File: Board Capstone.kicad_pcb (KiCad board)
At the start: 2 copper layers, 100 x 79 mm, 59 parts, among them J101 JST-ZH 4P, J102 HDR 02x20 2.54, J103 JST-ZH 2P, J104 JST-ZH 2P, J105 JST-ZH 3P, J106 JST-ZH 3P, J201 JST-XH 6P, Q101 FDV304P, Q102 BC847CLT3G, Q103 MMBT2907AL, Q104 MMBT2907AL, Q201 FDV301N, Q202 FDV301N, Q203 SSF3365, SW201 SW, U101 MCP3021, U102 SN74LV1T125DBV, U103 SN74LV1T125DBV, U201 LM2678SX-5.0, U202 BQ7720700DSSR, U203 LM2675M-12

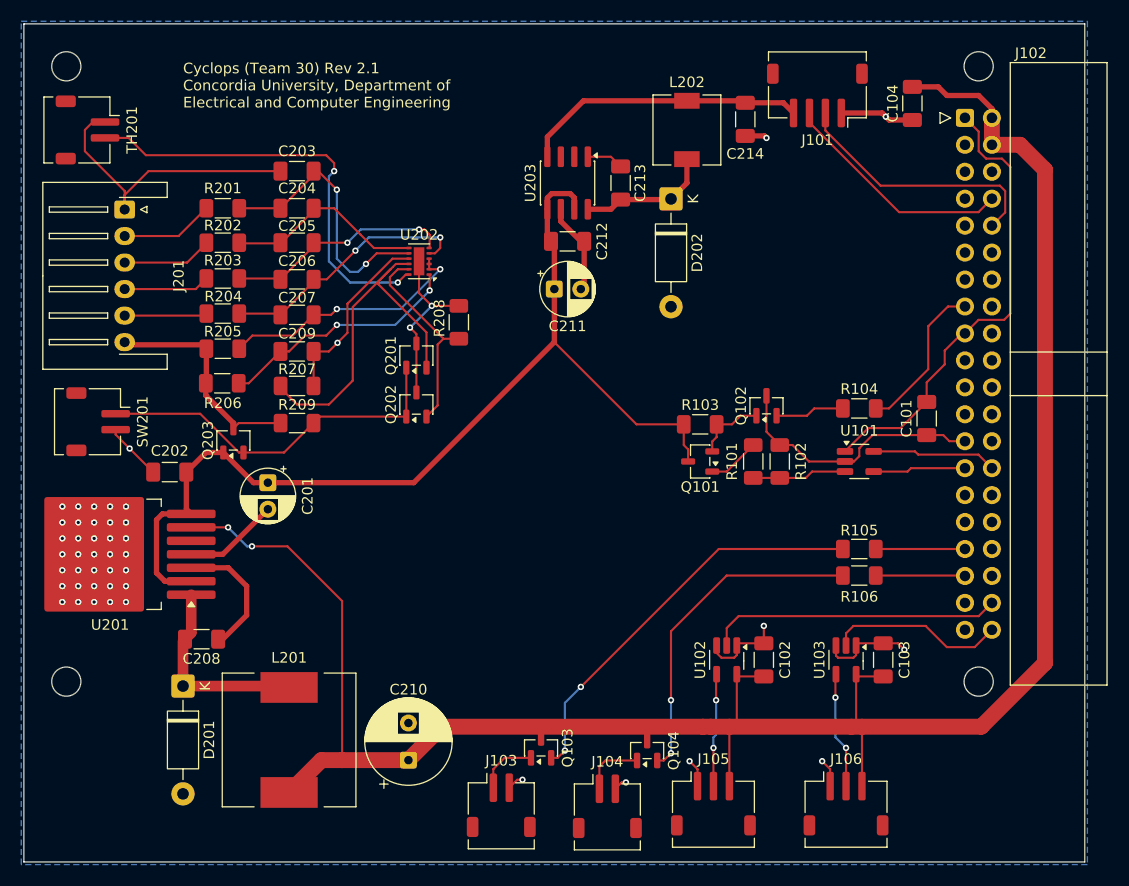
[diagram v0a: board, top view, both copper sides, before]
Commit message: Rev 2.2 Added test point and status LED
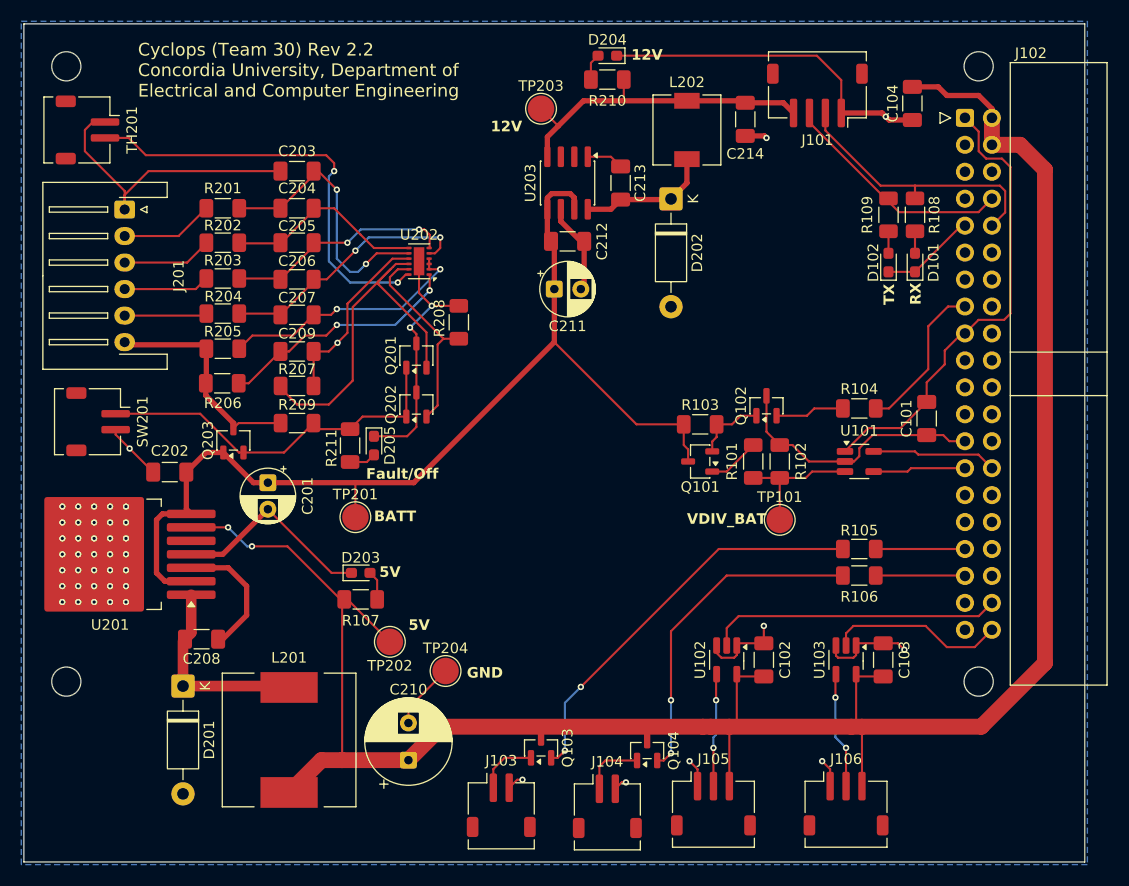
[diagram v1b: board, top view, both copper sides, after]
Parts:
- added D101: AMBER, LED_SMD:LED_0603_1608Metric_Pad1.05x0.95mm_HandSolder, F.Cu at (134.0, 72.5)
- added D102: AMBER, LED_SMD:LED_0603_1608Metric_Pad1.05x0.95mm_HandSolder, F.Cu at (131.5, 72.5)
- added D203: RED, LED_SMD:LED_0603_1608Metric_Pad1.05x0.95mm_HandSolder, F.Cu at (81.8, 101.8)
- added D204: RED, LED_SMD:LED_0603_1608Metric_Pad1.05x0.95mm_HandSolder, F.Cu at (105.0, 53.0)
- added D205: RED, LED_SMD:LED_0603_1608Metric_Pad1.05x0.95mm_HandSolder, F.Cu at (83.0, 89.8)
- added R107: 5k, Resistor_SMD:R_1206_3216Metric_Pad1.30x1.75mm_HandSolder, F.Cu at (81.8, 104.2)
- added R108: 1.5k, Resistor_SMD:R_1206_3216Metric_Pad1.30x1.75mm_HandSolder, F.Cu at (134.0, 68.0)
- added R109: 1.5k, Resistor_SMD:R_1206_3216Metric_Pad1.30x1.75mm_HandSolder, F.Cu at (131.5, 68.0)
- added R210: 12k, Resistor_SMD:R_1206_3216Metric_Pad1.30x1.75mm_HandSolder, F.Cu at (105.0, 55.2)
- added R211: 20k, Resistor_SMD:R_1206_3216Metric_Pad1.30x1.75mm_HandSolder, F.Cu at (80.8, 89.8)
- added TP101: ~, TestPoint:TestPoint_Pad_D2.5mm, F.Cu at (121.2, 96.8)
- added TP201: ~, TestPoint:TestPoint_Pad_D2.5mm, F.Cu at (81.2, 96.5)
- added TP202: ~, TestPoint:TestPoint_Pad_D2.5mm, F.Cu at (84.5, 108.2)
- added TP203: ~, TestPoint:TestPoint_Pad_D2.5mm, F.Cu at (98.8, 58.0)
- added TP204: GND, TestPoint:TestPoint_Pad_D2.5mm, F.Cu at (89.8, 111.0)
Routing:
- net GND: track 144.5 -> 203.1 mm
- net +5V: track 199.4 -> 205.4 mm
- net +12V: track 27.0 -> 31.3 mm
- net Net-(U101-AIN): track 8.90 -> 12.8 mm
- net +BATT: track 95.3 -> 98.6 mm
- net Net-(D203-A): track 0.00 -> 2.78 mm
- net Net-(D205-A): track 0.00 -> 2.53 mm
- net Net-(D204-A): track 0.00 -> 2.53 mm
- net Net-(D102-A): track 0.00 -> 2.08 mm
- net Net-(D101-A): track 0.00 -> 2.08 mm
- net /UART_RX: track 24.7 -> 25.9 mm
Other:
- board text added: "12V"
- board text added: "5V"
- board text added: "BATT"
- board text added: "Cyclops (Team 30) Rev 2.2 Concordia University, Department of Electrical and Computer Engineering"
- board text added: "Fault/Off"
- board text added: "GND"
- board text added: "RX"
- board text added: "TX"
- board text added: "VDIV_BAT"
- board text removed: "Cyclops (Team 30) Rev 2.1 Concordia University, Department of Electrical and Computer Engineering"

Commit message: Rev 2.4
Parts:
- removed C101, C102, C103, C203, C204, C205, C206, C207, C209: 0.1uF, Capacitor_SMD:C_1206_3216Metric_Pad1.33x1.80mm_HandSolder
- removed C104: 10uF, Capacitor_SMD:C_1206_3216Metric_Pad1.33x1.80mm_HandSolder
- removed C201, C211: 15uF, Capacitor_THT:CP_Radial_D5.0mm_P2.50mm
- removed C202, C212: 1uF, Capacitor_SMD:C_1206_3216Metric_Pad1.33x1.80mm_HandSolder
- removed C208, C213: 0.01uF, Capacitor_SMD:C_1206_3216Metric_Pad1.33x1.80mm_HandSolder
- removed C210: 180uF, Capacitor_THT:CP_Radial_D8.0mm_P3.50mm
- removed C214: 47uF, Capacitor_SMD:C_1206_3216Metric_Pad1.33x1.80mm_HandSolder
- removed D101, D102: AMBER, LED_SMD:LED_0603_1608Metric_Pad1.05x0.95mm_HandSolder
- removed D201, D202: ~, Diode_THT:D_DO-41_SOD81_P10.16mm_Horizontal
- removed D203, D204, D205: RED, LED_SMD:LED_0603_1608Metric_Pad1.05x0.95mm_HandSolder
- removed J101: JST-ZH 4P, Connector_JST:JST_ZH_S4B-ZR-SM4A-TF_1x04-1MP_P1.50mm_Horizontal
- removed J103, J104: JST-ZH 2P, Connector_JST:JST_ZH_S2B-ZR-SM4A-TF_1x02-1MP_P1.50mm_Horizontal
- removed J105, J106: JST-ZH 3P, Connector_JST:JST_ZH_S3B-ZR-SM4A-TF_1x03-1MP_P1.50mm_Horizontal
- removed J201: JST-XH 6P, Connector_JST:JST_XH_S6B-XH-A-1_1x06_P2.50mm_Horizontal
- removed L201: 22uH, Inductor_SMD:L_12x12mm_H4.5mm
- removed L202: 22uH, Inductor_SMD:L_6.3x6.3_H3
- removed Q101: FDV304P, Package_TO_SOT_SMD:SOT-23-3
- removed Q102: BC847CLT3G, Package_TO_SOT_SMD:SOT-23
- removed Q103, Q104: MMBT2907AL, Package_TO_SOT_SMD:SOT-23
- removed Q201, Q202: FDV301N, Package_TO_SOT_SMD:SOT-23-3
- removed Q203: SSF3365, Package_TO_SOT_SMD:SOT-23-3
- removed R101, R103, R207, R208, R209: 10k, Resistor_SMD:R_1206_3216Metric_Pad1.30x1.75mm_HandSolder
- removed R102, R104, R105, R106, R201, R202, R203, R204, R205: 1k, Resistor_SMD:R_1206_3216Metric_Pad1.30x1.75mm_HandSolder
- removed R107: 5k, Resistor_SMD:R_1206_3216Metric_Pad1.30x1.75mm_HandSolder
- removed R108, R109: 1.5k, Resistor_SMD:R_1206_3216Metric_Pad1.30x1.75mm_HandSolder
- removed R206: 300, Resistor_SMD:R_1206_3216Metric_Pad1.30x1.75mm_HandSolder
- removed R210: 12k, Resistor_SMD:R_1206_3216Metric_Pad1.30x1.75mm_HandSolder
- removed R211: 20k, Resistor_SMD:R_1206_3216Metric_Pad1.30x1.75mm_HandSolder
- removed SW201: SW, Connector_JST:JST_ZH_S2B-ZR-SM4A-TF_1x02-1MP_P1.50mm_Horizontal
- removed TH201: NTC 10k, Connector_JST:JST_ZH_S2B-ZR-SM4A-TF_1x02-1MP_P1.50mm_Horizontal
- removed TP101, TP201, TP202, TP203: ~, TestPoint:TestPoint_Pad_D2.5mm
- removed TP204: GND, TestPoint:TestPoint_Pad_D2.5mm
- removed U101: MCP3021, Package_TO_SOT_SMD:SOT-23-5_HandSoldering
- removed U102, U103: SN74LV1T125DBV, Package_TO_SOT_SMD:SOT-23-5_HandSoldering
- removed U201: LM2678SX-5.0, Package_TO_SOT_SMD:TO-263-7_TabPin4
- removed U202: BQ7720700DSSR, Package_SON:WSON-12-1EP_3x2mm_P0.5mm_EP1x2.65
- removed U203: LM2675M-12, Package_SO:SOIC-8_3.9x4.9mm_P1.27mm
- added C1: 10uF, Capacitor_SMD:C_0805_2012Metric_Pad1.18x1.45mm_HandSolder, F.Cu at (77.5, 118.2)
- added C10: 1uF, Capacitor_SMD:C_0805_2012Metric_Pad1.18x1.45mm_HandSolder, F.Cu at (102.5, 116.5)
- added C11: 47uF, Capacitor_SMD:C_0805_2012Metric_Pad1.18x1.45mm_HandSolder, F.Cu at (105.8, 84.5)
- added C12: 220nF, Capacitor_SMD:C_0805_2012Metric_Pad1.18x1.45mm_HandSolder, F.Cu at (72.5, 75.0)
- added C13: 220nF, Capacitor_SMD:C_0805_2012Metric_Pad1.18x1.45mm_HandSolder, F.Cu at (72.5, 72.5)
- added C14: 220nF, Capacitor_SMD:C_0805_2012Metric_Pad1.18x1.45mm_HandSolder, F.Cu at (72.5, 70.0)
- added C15: 220nF, Capacitor_SMD:C_0805_2012Metric_Pad1.18x1.45mm_HandSolder, F.Cu at (72.5, 67.5)
- added C16: 220nF, Capacitor_SMD:C_0805_2012Metric_Pad1.18x1.45mm_HandSolder, F.Cu at (72.5, 65.0)
- added C17: 220nF, Capacitor_SMD:C_0805_2012Metric_Pad1.18x1.45mm_HandSolder, F.Cu at (72.5, 62.5)
- added C18: 1uF, Capacitor_SMD:C_0805_2012Metric_Pad1.18x1.45mm_HandSolder, F.Cu at (109.2, 84.5)
- added C19: 220nF, Capacitor_SMD:C_0805_2012Metric_Pad1.18x1.45mm_HandSolder, F.Cu at (72.5, 77.5)
- added C2: 0.1uF, Capacitor_SMD:C_0805_2012Metric_Pad1.18x1.45mm_HandSolder, F.Cu at (111.8, 91.2)
- added C20: 0.01uF, Capacitor_SMD:C_0805_2012Metric_Pad1.18x1.45mm_HandSolder, F.Cu at (116.2, 72.2)
- added C21: 1uF, Capacitor_SMD:C_0805_2012Metric_Pad1.18x1.45mm_HandSolder, F.Cu at (87.2, 72.8)
- added C22: 100pF, Capacitor_SMD:C_0805_2012Metric_Pad1.18x1.45mm_HandSolder, F.Cu at (84.2, 85.2)
- added C23: 180uF, Capacitor_THT:CP_Radial_D8.0mm_P3.50mm, F.Cu at (118.0, 57.0)
- added C24: 1uF, Capacitor_SMD:C_0805_2012Metric_Pad1.18x1.45mm_HandSolder, F.Cu at (82.8, 72.8)
- added C25: 47uF, Capacitor_SMD:C_0805_2012Metric_Pad1.18x1.45mm_HandSolder, F.Cu at (75.5, 107.5)
- added C26: 1uF, Capacitor_SMD:C_0805_2012Metric_Pad1.18x1.45mm_HandSolder, F.Cu at (71.5, 107.5)
- added C27: 0.01uF, Capacitor_SMD:C_0805_2012Metric_Pad1.18x1.45mm_HandSolder, F.Cu at (65.5, 113.5)
- added C28: 47uF, Capacitor_SMD:C_0805_2012Metric_Pad1.18x1.45mm_HandSolder, F.Cu at (75.5, 113.5)
- added C29: 1uF, Capacitor_SMD:C_0805_2012Metric_Pad1.18x1.45mm_HandSolder, F.Cu at (117.2, 98.2)
- added C3: 1uF, Capacitor_SMD:C_0805_2012Metric_Pad1.18x1.45mm_HandSolder, F.Cu at (121.7, 115.0)
- added C4: 1uF, Capacitor_SMD:C_0805_2012Metric_Pad1.18x1.45mm_HandSolder, F.Cu at (136.5, 115.0)
- added C5: 1uF, Capacitor_SMD:C_0805_2012Metric_Pad1.18x1.45mm_HandSolder, F.Cu at (135.5, 63.0)
- added C6: 10uF, Capacitor_SMD:C_0805_2012Metric_Pad1.18x1.45mm_HandSolder, F.Cu at (135.5, 59.0)
- added C7: 0.1uF, Capacitor_SMD:C_0805_2012Metric_Pad1.18x1.45mm_HandSolder, F.Cu at (91.5, 111.5)
- added C8: 0.1uF, Capacitor_SMD:C_0805_2012Metric_Pad1.18x1.45mm_HandSolder, F.Cu at (106.5, 111.5)
- added C9: 1uF, Capacitor_SMD:C_0805_2012Metric_Pad1.18x1.45mm_HandSolder, F.Cu at (87.5, 116.5)
- added D10: D_Zener, Diode_SMD:D_0805_2012Metric_Pad1.15x1.40mm_HandSolder, F.Cu at (117.2, 101.2)
- added D3: 1N4148W, Diode_SMD:D_SOD-123, F.Cu at (86.5, 64.5)
- added D4: SK35, Diode_SMD:D_SMB-SMC_Universal_Handsoldering, F.Cu at (117.0, 67.0)
- added D5: 1N4148W, Diode_SMD:D_SOD-123, F.Cu at (83.5, 64.5)
- added D7: SK15, Diode_SMD:D_SMA-SMB_Universal_Handsoldering, F.Cu at (61.0, 106.5)
- added D8: QBLP601-R35, LED_SMD:LED_0603_1608Metric_Pad1.05x0.95mm_HandSolder, F.Cu at (97.0, 83.0)
- added J1: JST-ZH 4P, Connector_JST:JST_ZH_S4B-ZR-SM4A-TF_1x04-1MP_P1.50mm_Horizontal, F.Cu at (72.5, 123.0)
- added J2: JST-ZH 2P, Connector_JST:JST_ZH_S2B-ZR-SM4A-TF_1x02-1MP_P1.50mm_Horizontal, F.Cu at (117.7, 123.0)
- added J3: JST-ZH 2P, Connector_JST:JST_ZH_S2B-ZR-SM4A-TF_1x02-1MP_P1.50mm_Horizontal, F.Cu at (132.5, 123.0)
- added J5: JST-ZH 3P, Connector_JST:JST_ZH_S3B-ZR-SM4A-TF_1x03-1MP_P1.50mm_Horizontal, F.Cu at (87.5, 123.0)
- added J6: JST-ZH 3P, Connector_JST:JST_ZH_S3B-ZR-SM4A-TF_1x03-1MP_P1.50mm_Horizontal, F.Cu at (102.5, 123.0)
- added J7: JST-XH 7P, Connector_JST:JST_XH_S7B-XH-A_1x07_P2.50mm_Horizontal, F.Cu at (60.0, 62.5)
- added J8: XT60, Connector_AMASS:AMASS_XT60PW-F_1x02_P7.20mm_Horizontal, F.Cu at (66.0, 90.2)
- added J9: 01x03_Pin, Connector_PinHeader_2.54mm:PinHeader_1x03_P2.54mm_Horizontal, F.Cu at (92.6, 73.5)
- added JP1: SolderJumper_2_Open, Jumper:SolderJumper-2_P1.3mm_Open_RoundedPad1.0x1.5mm, F.Cu at (123.2, 94.2)
- added JP2: SolderJumper_2_Open, Jumper:SolderJumper-2_P1.3mm_Open_RoundedPad1.0x1.5mm, F.Cu at (126.2, 94.2)
- added L1: 22uH, Inductor_SMD:L_12x12mm_H4.5mm, F.Cu at (104.0, 62.0)
- added L2: 22uH, Inductor_SMD:L_6.3x6.3_H3, F.Cu at (59.5, 113.5)
- added Q2: FDV304P, Package_TO_SOT_SMD:SOT-23-3, F.Cu at (92.5, 90.0)
- added R1: 10k, Resistor_SMD:R_0805_2012Metric_Pad1.20x1.40mm_HandSolder, F.Cu at (112.8, 95.2)
- added R10: 10, Resistor_SMD:R_0805_2012Metric_Pad1.20x1.40mm_HandSolder, F.Cu at (67.0, 70.0)
- added R11: 10, Resistor_SMD:R_0805_2012Metric_Pad1.20x1.40mm_HandSolder, F.Cu at (67.0, 67.5)
- added R12: 10, Resistor_SMD:R_0805_2012Metric_Pad1.20x1.40mm_HandSolder, F.Cu at (67.0, 65.0)
- added R13: 10, Resistor_SMD:R_0805_2012Metric_Pad1.20x1.40mm_HandSolder, F.Cu at (67.0, 62.5)
- added R14: 10, Resistor_SMD:R_0805_2012Metric_Pad1.20x1.40mm_HandSolder, F.Cu at (87.2, 69.5)
- added R15: 100, Resistor_SMD:R_0805_2012Metric_Pad1.20x1.40mm_HandSolder, F.Cu at (83.2, 88.2)
- added R16: 0.001, Resistor_SMD:R_1206_3216Metric_Pad1.30x1.75mm_HandSolder, F.Cu at (84.2, 91.5)
- added R17: 100, Resistor_SMD:R_0805_2012Metric_Pad1.20x1.40mm_HandSolder, F.Cu at (85.2, 88.2)
- added R18: 100, Resistor_SMD:R_0805_2012Metric_Pad1.20x1.40mm_HandSolder, F.Cu at (82.8, 69.5)
- added R2: 1k, Resistor_SMD:R_0805_2012Metric_Pad1.20x1.40mm_HandSolder, F.Cu at (117.2, 95.2)
- added R20: 10M, Resistor_SMD:R_0805_2012Metric_Pad1.20x1.40mm_HandSolder, F.Cu at (89.5, 89.8)
- added R21: 4.7k, Resistor_SMD:R_0805_2012Metric_Pad1.20x1.40mm_HandSolder, F.Cu at (96.2, 86.2)
- added R3: 680, Resistor_SMD:R_0805_2012Metric_Pad1.20x1.40mm_HandSolder, F.Cu at (113.7, 115.0)
- added R4: 680, Resistor_SMD:R_0805_2012Metric_Pad1.20x1.40mm_HandSolder, F.Cu at (128.5, 115.0)
- added R7: 10, Resistor_SMD:R_0805_2012Metric_Pad1.20x1.40mm_HandSolder, F.Cu at (67.0, 77.5)
- added R8: 10, Resistor_SMD:R_0805_2012Metric_Pad1.20x1.40mm_HandSolder, F.Cu at (67.0, 75.0)
- added R9: 10, Resistor_SMD:R_0805_2012Metric_Pad1.20x1.40mm_HandSolder, F.Cu at (67.0, 72.5)
- added SW1: RA11131100, TestPoint:TestPoint_2Pads_Pitch5.08mm_Drill1.3mm, F.Cu at (72.5, 90.0)
- added TH1: NTC 10k, Connector_JST:JST_ZH_S2B-ZR-SM4A-TF_1x02-1MP_P1.50mm_Horizontal, F.Cu at (91.0, 55.5)
- added TP1: ~, TestPoint:TestPoint_Pad_D1.5mm, F.Cu at (112.8, 98.2)
- added TP2: ~, TestPoint:TestPoint_Pad_D1.5mm, F.Cu at (72.8, 99.0)
- added TP3: ~, TestPoint:TestPoint_Pad_D1.5mm, F.Cu at (127.0, 56.8)
- added TP4: ~, TestPoint:TestPoint_Pad_D1.5mm, F.Cu at (74.0, 117.0)
- added U1: MCP3021, Package_TO_SOT_SMD:SOT-23-5_HandSoldering, F.Cu at (116.2, 91.2)
- added U2: TPS22917DBV, Package_TO_SOT_SMD:SOT-23-6, F.Cu at (117.7, 115.0)
- added U3: TPS22917DBV, Package_TO_SOT_SMD:SOT-23-6, F.Cu at (132.5, 115.0)
- added U4: SN74LV1T125DBV, Package_TO_SOT_SMD:SOT-23-5_HandSoldering, F.Cu at (87.5, 111.5)
- added U5: SN74LV1T125DBV, Package_TO_SOT_SMD:SOT-23-5_HandSoldering, F.Cu at (102.5, 111.5)
- added U6: LM2678SX-5.0, Package_TO_SOT_SMD:TO-263-7_TabPin4, F.Cu at (121.7, 80.0)
- added U7: BQ77307RGRR, Package_DFN_QFN:Texas_RGP0020D_VQFN-20-1EP_4x4mm_P0.5mm_EP2.7x2.7mm, F.Cu at (85.0, 80.0)
- added U8: LM2675M-12, Package_SO:SOIC-8_3.9x4.9mm_P1.27mm, F.Cu at (70.0, 113.5)
- renumbered J102 to J4
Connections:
- J4 pad 15: /Voltage Div EN -> unconnected-(J4-Pin_15-Pad15)
- J4 pad 33: /Vibration0 ~{EN} -> /Vibration0
- J4 pad 35: /Vibration1 ~{EN} -> /Vibration1
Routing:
- net GND: track 203.1 -> 83.2 mm, vias 47 -> 37
- net /UART_TX: track 22.1 -> 137.7 mm
- net /UART_RX: track 25.9 -> 141.4 mm, vias 0 -> 1
- net /Power/PACK-: track 0.00 -> 79.1 mm, vias 0 -> 4
- net /Power/SCL: track 0.00 -> 66.1 mm, vias 0 -> 1
- net /Power/SDA: track 0.00 -> 61.8 mm, vias 0 -> 1
- net Net-(U202-TS): track 40.7 -> 0.00 mm, vias 2 -> 0
- net Net-(Q103-B): track 38.3 -> 0.00 mm, vias 2 -> 0
- net Net-(Q201-D): track 35.4 -> 0.00 mm
- net Net-(Q201-G): track 34.1 -> 0.00 mm
- net /Status_LED_Data: track 27.6 -> 59.6 mm, vias 0 -> 1
- net Net-(Q104-B): track 31.5 -> 0.00 mm, vias 2 -> 0
- net +12V: track 31.3 -> 0.00 mm
- net /Vibration0: track 0.00 -> 30.9 mm
- net Net-(U7A-TS): track 0.00 -> 30.1 mm, vias 0 -> 2
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- added copper zone on F.Cu, net +12V
- added copper zone on F.Cu, net +5V
- added copper zone on F.Cu, net +BATT
- added copper zone on F.Cu, net /Power/PACK-
- added copper zone on F.Cu, net GND
- added copper zone on F.Cu, net Net-(D4-K)
- added copper zone on F.Cu, net Net-(D7-K)
- added copper zone on F.Cu, net Net-(J8-Pin_1)
- added copper zone on F.Cu, net Net-(Q2-S)
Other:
- board text added: "Concordia University, Department of Electrical and Computer Engineering Cyclops (Team 30) PCB Rev: 2.4 2026-02-03"
- board text removed: "12V"
- board text removed: "5V"
- board text removed: "BATT"
- board text removed: "Cyclops (Team 30) Rev 2.2 Concordia University, Department of Electrical and Computer Engineering"
- board text removed: "Fault/Off"
- board text removed: "GND"
- board text removed: "RX"
- board text removed: "TX"
- board text removed: "VDIV_BAT"
